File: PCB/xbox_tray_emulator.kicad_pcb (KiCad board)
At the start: 2 copper layers, 10.2 x 26.4 mm, 4 parts, among them J1 to Xbox, U1 ATtiny13A-S

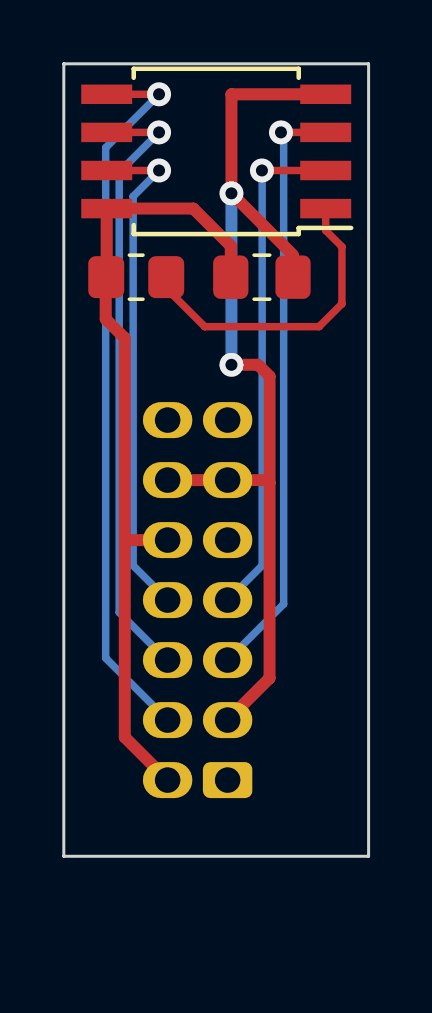
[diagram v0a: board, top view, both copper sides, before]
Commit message: reduce sleep current from 200uA to 50uA
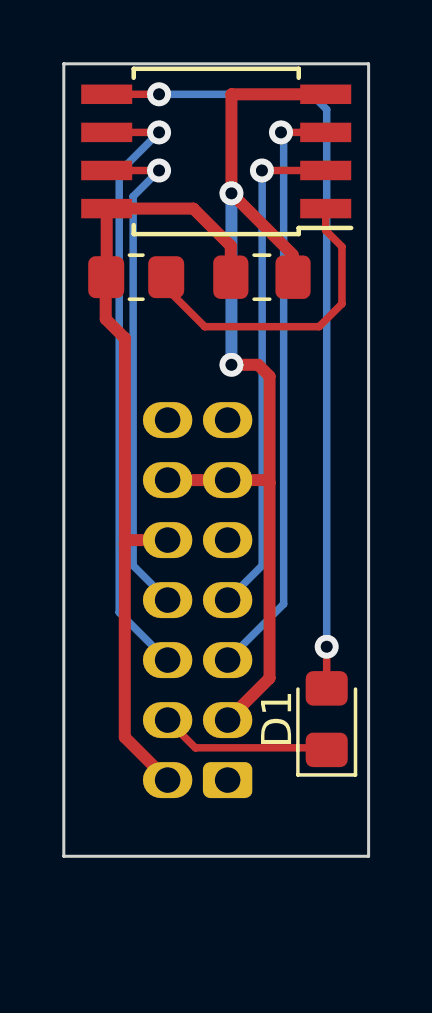
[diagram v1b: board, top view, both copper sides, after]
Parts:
- added D1: 1N4148, Diode_SMD:D_0805_2012Metric_Pad1.15x1.40mm_HandSolder, F.Cu at (145.9, 78.6)
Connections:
- J1 pad 4: Net-(J1-Pad4) -> Net-(D1-Pad1)
- U1 pad 5: Net-(J1-Pad4) -> Net-(D1-Pad2)
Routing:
- net Net-(D1-Pad2): track 0.00 -> 26.8 mm, vias 0 -> 2
- net Net-(J1-Pad4): track 24.2 -> 0.00 mm, vias 1 -> 0
- net Net-(D1-Pad1): track 0.00 -> 5.71 mm
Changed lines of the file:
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@@
   (net 4 "unconnected-(J1-Pad9)")
   (net 5 "unconnected-(J1-Pad13)")
-  (net 6 "Net-(J1-Pad4)")
+  (net 6 "Net-(D1-Pad1)")
   (net 7 "Net-(J1-Pad5)")
   (net 8 "Net-(J1-Pad6)")
@@
   (net 10 "Net-(J1-Pad8)")
   (net 11 "Net-(R1-Pad1)")
+  (net 12 "Net-(D1-Pad2)")
   (footprint "Capacitor_SMD:C_0805_2012Metric_Pad1.18x1.45mm_HandSolder" (layer "F.Cu")
     (at 143.764 63.881 180)
@@
       (net 2 "Net-(C1-Pad2)") (pintype "passive"))
     (model "${KICAD6_3DMODEL_DIR}/Capacitor_SMD.3dshapes/C_0805_2012Metric.wrl"
+      (offset (xyz 0 0 0))
+      (scale (xyz 1 1 1))
+      (rotate (xyz 0 0 0))
+    )
+  )
+  (footprint "Diode_SMD:D_0805_2012Metric_Pad1.15x1.40mm_HandSolder" (layer "F.Cu")
+    (at 145.923 78.613 90)
+    (descr "Diode SMD 0805 (2012 Metric), square (rectangular) end terminal, IPC_7351 nominal, (Body size source: https://docs.google.com/spreadsheets/d/1BsfQQcO9C6DZCsRaXUlFlo91Tg2WpOkGARC1WS5S8t0/edit?usp=sharing), generated with kicad-footprint-generator")
+    (tags "diode handsolder")
+    (property "Sheetfile" "xbox_tray_emulator.kicad_sch")
+    (property "Sheetname" "")
+    (attr smd)
+    (fp_text reference "D1" (at 0 -1.65 90) (layer "F.SilkS")
+      (effects (font (size 1 1) (thickness 0.15)))
+    )
+    (fp_text value "1N4148" (at 0 1.65 90) (layer "F.Fab")
+      (effects (font (size 1 1) (thickness 0.15)))
+    )
+    (fp_text user "${REFERENCE}" (at 0 0 90) (layer "F.Fab")
+      (effects (font (size 0.5 0.5) (thickness 0.08)))
+    )
+    (fp_line (start -1.86 -0.96) (end -1.86 0.96) (layer "F.SilkS") (width 0.12))
+    (fp_line (start 1 -0.96) (end -1.86 -0.96) (layer "F.SilkS") (width 0.12))
+    (fp_line (start -1.86 0.96) (end 1 0.96) (layer "F.SilkS") (width 0.12))
+    (fp_line (start 1.85 -0.95) (end 1.85 0.95) (layer "F.CrtYd") (width 0.05))
+    (fp_line (start 1.85 0.95) (end -1.85 0.95) (layer "F.CrtYd") (width 0.05))
+    (fp_line (start -1.85 0.95) (end -1.85 -0.95) (layer "F.CrtYd") (width 0.05))
+    (fp_line (start -1.85 -0.95) (end 1.85 -0.95) (layer "F.CrtYd") (width 0.05))
+    (fp_line (start 1 0.6) (end 1 -0.6) (layer "F.Fab") (width 0.1))
+    (fp_line (start -1 0.6) (end 1 0.6) (layer "F.Fab") (width 0.1))
+    (fp_line (start 1 -0.6) (end -0.7 -0.6) (layer "F.Fab") (width 0.1))
+    (fp_line (start -0.7 -0.6) (end -1 -0.3) (layer "F.Fab") (width 0.1))
+    (fp_line (start -1 -0.3) (end -1 0.6) (layer "F.Fab") (width 0.1))
+    (pad "1" smd roundrect (at -1.025 0 90) (size 1.15 1.4) (layers "F.Cu" "F.Paste" "F.Mask") (roundrect_rratio 0.217391)
+      (net 6 "Net-(D1-Pad1)") (pinfunction "K") (pintype "passive"))
+    (pad "2" smd roundrect (at 1.025 0 90) (size 1.15 1.4) (layers "F.Cu" "F.Paste" "F.Mask") (roundrect_rratio 0.217391)
+      (net 12 "Net-(D1-Pad2)") (pinfunction "A") (pintype "passive"))
+    (model "${KICAD6_3DMODEL_DIR}/Diode_SMD.3dshapes/D_0805_2012Metric.wrl"
       (offset (xyz 0 0 0))
       (scale (xyz 1 1 1))
@@
       (net 1 "Net-(C1-Pad1)") (pinfunction "GND") (pintype "power_in"))
     (pad "5" smd rect (at 3.65 1.905 180) (size 1.7 0.65) (layers "F.Cu" "F.Paste" "F.Mask")
-      (net 6 "Net-(J1-Pad4)") (pinfunction "PB0") (pintype "bidirectional"))
+      (net 12 "Net-(D1-Pad2)") (pinfunction "PB0") (pintype "bidirectional"))
     (pad "6" smd rect (at 3.65 0.635 180) (size 1.7 0.65) (layers "F.Cu" "F.Paste" "F.Mask")
       (net 8 "Net-(J1-Pad6)") (pinfunction "PB1") (pintype "bidirectional"))
@@
       (net 1 "Net-(C1-Pad1)") (pinfunction "Pin_3") (pintype "passive"))
     (pad "4" thru_hole oval (at 2 -2 90) (size 1.2 1.65) (drill 0.85) (layers *.Cu *.Mask)
-      (net 6 "Net-(J1-Pad4)") (pinfunction "Pin_4") (pintype "passive"))
+      (net 6 "Net-(D1-Pad1)") (pinfunction "Pin_4") (pintype "passive"))
     (pad "5" thru_hole oval (at 4 0 90) (size 1.2 1.65) (drill 0.85) (layers *.Cu *.Mask)
       (net 7 "Net-(J1-Pad5)") (pinfunction "Pin_5") (pintype "passive"))
@@
   (segment (start 139.192 65.913) (end 139.192 79.216) (width 0.4) (layer "F.Cu") (net 2))
   (segment (start 142.7265 62.8435) (end 141.478 61.595) (width 0.4) (layer "F.Cu") (net 2))
-  (segment (start 138.59 57.785) (end 140.335 57.785) (width 0.25) (layer "F.Cu") (net 6))
-  (via (at 140.335 57.785) (size 0.8) (drill 0.4) (layers "F.Cu" "B.Cu") (net 6))
-  (segment (start 138.557 76.581) (end 140.621 78.645) (width 0.25) (layer "B.Cu") (net 6))
-  (segment (start 138.557 59.563) (end 138.557 76.581) (width 0.25) (layer "B.Cu") (net 6))
-  (segment (start 140.335 57.785) (end 138.557 59.563) (width 0.25) (layer "B.Cu") (net 6))
+  (segment (start 140.621 78.645) (end 141.54552 79.56952) (width 0.25) (layer "F.Cu") (net 6))
+  (segment (start 145.85452 79.56952) (end 145.923 79.638) (width 0.25) (layer "F.Cu") (net 6))
+  (segment (start 141.54552 79.56952) (end 145.85452 79.56952) (width 0.25) (layer "F.Cu") (net 6))
   (segment (start 145.89 59.055) (end 144.399 59.055) (width 0.25) (layer "F.Cu") (net 7))
   (via (at 144.399 59.055) (size 0.8) (drill 0.4) (layers "F.Cu" "B.Cu") (net 7))
@@
   (segment (start 141.859 65.532) (end 140.573 64.246) (width 0.25) (layer "F.Cu") (net 11))
   (segment (start 145.669 65.532) (end 141.859 65.532) (width 0.25) (layer "F.Cu") (net 11))
+  (segment (start 145.923 77.588) (end 145.923 76.2) (width 0.25) (layer "F.Cu") (net 12))
+  (segment (start 138.59 57.785) (end 140.335 57.785) (width 0.25) (layer "F.Cu") (net 12))
+  (via (at 145.923 76.2) (size 0.8) (drill 0.4) (layers "F.Cu" "B.Cu") (net 12))
+  (via (at 140.335 57.785) (size 0.8) (drill 0.4) (layers "F.Cu" "B.Cu") (net 12))
+  (segment (start 145.923 76.2) (end 145.923 58.293) (width 0.25) (layer "B.Cu") (net 12))
+  (segment (start 145.415 57.785) (end 140.335 57.785) (width 0.25) (layer "B.Cu") (net 12))
+  (segment (start 145.923 58.293) (end 145.415 57.785) (width 0.25) (layer "B.Cu") (net 12))
 )

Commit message: Xbox DVD logic levels are 3.3v, a 3.3v regulator was added to the PCB so the ATtiny13a will output and accept 3.3v logic. ATtiny13a sleep current draw is now a fration of a uA. modify tray open sequence to closer approximate a real DVD drive.
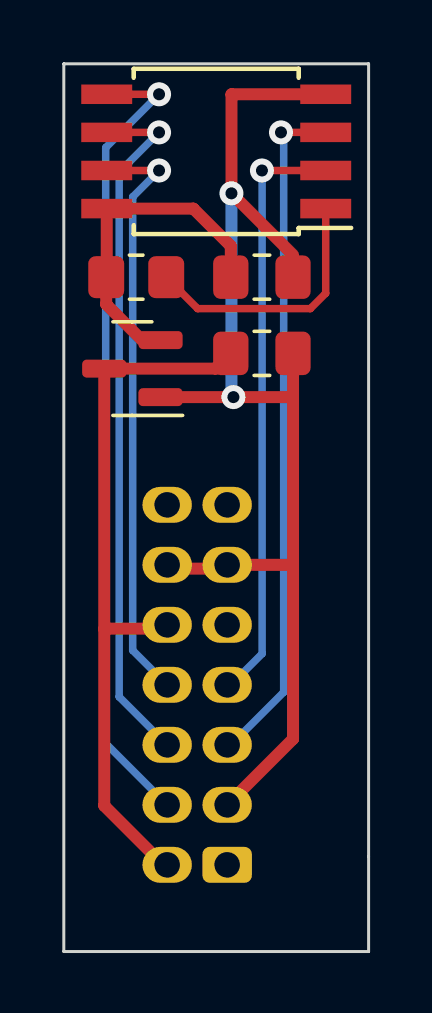
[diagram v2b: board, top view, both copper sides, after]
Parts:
- removed D1: 1N4148, Diode_SMD:D_0805_2012Metric_Pad1.15x1.40mm_HandSolder
- added C2: 1uf, Capacitor_SMD:C_0805_2012Metric_Pad1.18x1.45mm_HandSolder, F.Cu at (143.8, 66.4)
- added U2: AP2127N-3.3, Package_TO_SOT_SMD:SOT-23, F.Cu at (139.4, 66.9)
- C1: value 0.47uf -> 4.7uf
- moved J1 2.83 mm to (142.6, 83.5)
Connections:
- J1 pad 10: Net-(C1-Pad2) -> Net-(J1-Pad10)
- J1 pad 2: Net-(C1-Pad2) -> Net-(J1-Pad10)
- J1 pad 4: Net-(D1-Pad1) -> Net-(J1-Pad4)
- U1 pad 5: Net-(D1-Pad2) -> Net-(J1-Pad4)
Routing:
- net Net-(J1-Pad4): track 0.00 -> 27.0 mm, vias 0 -> 1
- net Net-(D1-Pad2): track 26.8 -> 0.00 mm, vias 2 -> 0
- net Net-(J1-Pad10): track 0.00 -> 24.1 mm
- net Net-(C1-Pad2): track 27.1 -> 11.4 mm
- net Net-(C1-Pad1): track 32.7 -> 41.3 mm
- net Net-(D1-Pad1): track 5.71 -> 0.00 mm
- net Net-(J1-Pad7): track 16.9 -> 19.9 mm
- net Net-(J1-Pad5): track 19.9 -> 22.9 mm
- net Net-(J1-Pad8): track 16.9 -> 19.7 mm
- net Net-(J1-Pad6): track 20.6 -> 23.4 mm
- net Net-(R1-Pad1): track 10.5 -> 8.79 mm
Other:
- board size 10.2 x 26.4 mm -> 10.2 x 29.6 mm

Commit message: add ground fill
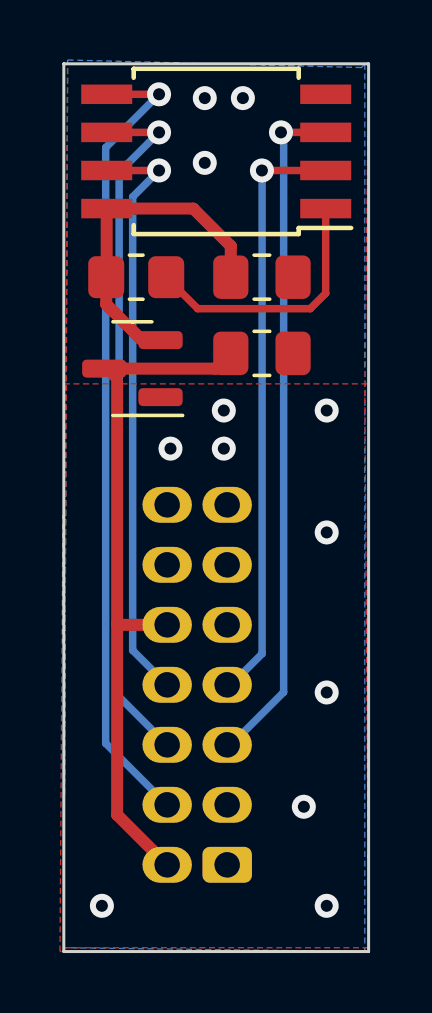
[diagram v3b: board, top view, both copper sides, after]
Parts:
- C1: value 4.7uf -> 1uf
- turned C1 to 0 degrees
- turned R1 to 0 degrees
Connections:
- C1 pad 1: Net-(C1-Pad1) -> /Net-(R1-Pad1)
- C2 pad 2: Net-(C1-Pad1) -> Net-(C1-Pad2)
- J1 pad 11: Net-(C1-Pad1) -> Net-(C1-Pad2)
- J1 pad 12: Net-(C1-Pad1) -> Net-(C1-Pad2)
- J1 pad 3: Net-(C1-Pad1) -> Net-(C1-Pad2)
- R1 pad 1: Net-(R1-Pad1) -> /Net-(R1-Pad1)
- R1 pad 2: Net-(C1-Pad2) -> Net-(R1-Pad2)
- U1 pad 1: Net-(R1-Pad1) -> Net-(R1-Pad2)
- U1 pad 4: Net-(C1-Pad1) -> Net-(C1-Pad2)
- U1 pad 8: Net-(C1-Pad2) -> /Net-(R1-Pad1)
- U2 pad 1: Net-(C1-Pad1) -> Net-(C1-Pad2)
- U2 pad 2: Net-(C1-Pad2) -> /Net-(R1-Pad1)
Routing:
- net Net-(C1-Pad1): track 41.3 -> 0.00 mm, vias 2 -> 0
- net Net-(C1-Pad2): track 11.4 -> 0.00 mm, vias 0 -> 12
- net /Net-(R1-Pad1): track 0.00 -> 11.4 mm
- net Net-(R1-Pad2): track 0.00 -> 8.79 mm
- net Net-(R1-Pad1): track 8.79 -> 0.00 mm
- net /Net-(J1-Pad10): track 24.1 -> 23.5 mm
- added copper zone on B.Cu, net Net-(C1-Pad2)
- added copper zone on F.Cu, net Net-(C1-Pad2)

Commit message: increase U1 pads for "narrow" ATtiny13
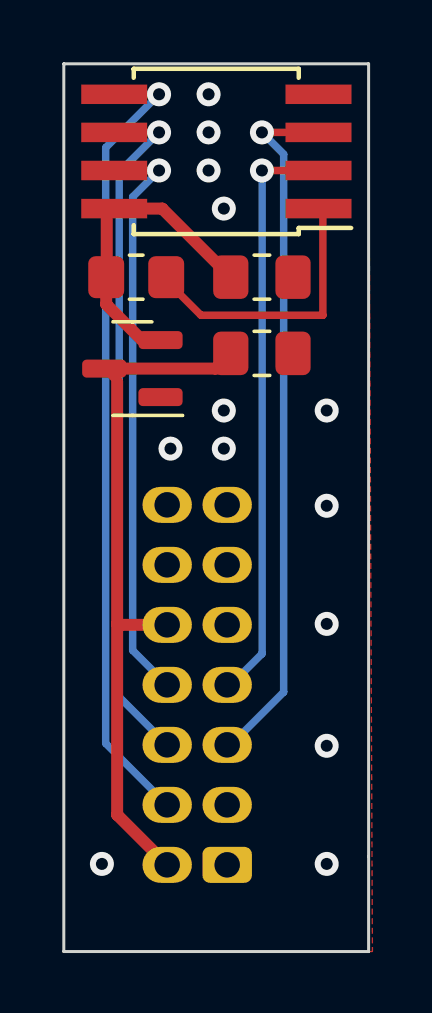
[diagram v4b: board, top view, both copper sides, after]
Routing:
- net /Net-(R1-Pad1): track 11.4 -> 10.6 mm
- net Net-(J1-Pad5): track 22.9 -> 23.5 mm
- net Net-(R1-Pad2): track 8.79 -> 9.43 mm
- net Net-(C1-Pad2): vias 12 -> 13
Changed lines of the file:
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@@
     (fp_line (start -2.65 2.65) (end -2.65 -1.65) (layer "F.Fab") (width 0.15))
     (fp_line (start 2.65 2.65) (end -2.65 2.65) (layer "F.Fab") (width 0.15))
-    (pad "1" smd rect (at -3.65 -1.905 180) (size 1.7 0.65) (layers "F.Cu" "F.Paste" "F.Mask")
+    (pad "1" smd rect (at -3.41 -1.905 180) (size 2.2 0.65) (layers "F.Cu" "F.Paste" "F.Mask")
       (net 9 "Net-(R1-Pad2)") (pinfunction "~{RESET}/PB5") (pintype "bidirectional"))
-    (pad "2" smd rect (at -3.65 -0.635 180) (size 1.7 0.65) (layers "F.Cu" "F.Paste" "F.Mask")
+    (pad "2" smd rect (at -3.41 -0.635 180) (size 2.2 0.65) (layers "F.Cu" "F.Paste" "F.Mask")
       (net 6 "Net-(J1-Pad7)") (pinfunction "PB3") (pintype "bidirectional"))
-    (pad "3" smd rect (at -3.65 0.635 180) (size 1.7 0.65) (layers "F.Cu" "F.Paste" "F.Mask")
+    (pad "3" smd rect (at -3.41 0.635 180) (size 2.2 0.65) (layers "F.Cu" "F.Paste" "F.Mask")
       (net 4 "Net-(J1-Pad5)") (pinfunction "PB4") (pintype "bidirectional"))
-    (pad "4" smd rect (at -3.65 1.905 180) (size 1.7 0.65) (layers "F.Cu" "F.Paste" "F.Mask")
+    (pad "4" smd rect (at -3.41 1.905 180) (size 2.2 0.65) (layers "F.Cu" "F.Paste" "F.Mask")
       (net 12 "Net-(C1-Pad2)") (pinfunction "GND") (pintype "power_in"))
-    (pad "5" smd rect (at 3.65 1.905 180) (size 1.7 0.65) (layers "F.Cu" "F.Paste" "F.Mask")
+    (pad "5" smd rect (at 3.4 1.905 180) (size 2.2 0.65) (layers "F.Cu" "F.Paste" "F.Mask")
       (net 8 "Net-(J1-Pad4)") (pinfunction "PB0") (pintype "bidirectional"))
-    (pad "6" smd rect (at 3.65 0.635 180) (size 1.7 0.65) (layers "F.Cu" "F.Paste" "F.Mask")
+    (pad "6" smd rect (at 3.4 0.635 180) (size 2.2 0.65) (layers "F.Cu" "F.Paste" "F.Mask")
       (net 5 "Net-(J1-Pad6)") (pinfunction "PB1") (pintype "bidirectional"))
-    (pad "7" smd rect (at 3.65 -0.635 180) (size 1.7 0.65) (layers "F.Cu" "F.Paste" "F.Mask")
+    (pad "7" smd rect (at 3.4 -0.635 180) (size 2.2 0.65) (layers "F.Cu" "F.Paste" "F.Mask")
       (net 7 "Net-(J1-Pad8)") (pinfunction "PB2") (pintype "bidirectional"))
-    (pad "8" smd rect (at 3.65 -1.905 180) (size 1.7 0.65) (layers "F.Cu" "F.Paste" "F.Mask")
+    (pad "8" smd rect (at 3.4 -1.905 180) (size 2.2 0.65) (layers "F.Cu" "F.Paste" "F.Mask")
       (net 10 "/Net-(R1-Pad1)") (pinfunction "VCC") (pintype "power_in"))
     (model "${KICAD6_3DMODEL_DIR}/Package_SO.3dshapes/SOIC-8W_5.3x5.3mm_P1.27mm.wrl"
@@
   (gr_line (start 147.32 83.185) (end 147.32 86.36) (layer "Edge.Cuts") (width 0.1))
   (gr_line (start 147.32 56.769) (end 147.32 83.185) (layer "Edge.Cuts") (width 0.1))
-  (segment (start 145.89 59.055) (end 144.399 59.055) (width 0.25) (layer "F.Cu") (net 4))
-  (via (at 144.399 59.055) (size 0.8) (drill 0.4) (layers "F.Cu" "B.Cu") (net 4))
+  (segment (start 145.65 59.055) (end 143.764 59.055) (width 0.25) (layer "F.Cu") (net 4))
+  (via (at 143.764 59.055) (size 0.8) (drill 0.4) (layers "F.Cu" "B.Cu") (net 4))
+  (segment (start 144.488511 77.713489) (end 144.488511 59.779511) (width 0.25) (layer "B.Cu") (net 4))
   (segment (start 144.488511 77.713489) (end 142.605 79.597) (width 0.25) (layer "B.Cu") (net 4))
-  (segment (start 144.399 59.055) (end 144.488511 59.144511) (width 0.25) (layer "B.Cu") (net 4))
-  (segment (start 144.488511 59.144511) (end 144.488511 77.713489) (width 0.25) (layer "B.Cu") (net 4))
+  (segment (start 144.488511 59.779511) (end 143.764 59.055) (width 0.25) (layer "B.Cu") (net 4))
   (segment (start 138.59 59.055) (end 140.335 59.055) (width 0.25) (layer "F.Cu") (net 5))
   (via (at 140.335 59.055) (size 0.8) (drill 0.4) (layers "F.Cu" "B.Cu") (net 5))
@@
   (segment (start 138.55644 59.56356) (end 138.55644 79.42144) (width 0.25) (layer "B.Cu") (net 8))
   (segment (start 140.335 57.785) (end 138.55644 59.56356) (width 0.25) (layer "B.Cu") (net 8))
-  (segment (start 141.62252 64.93052) (end 140.573 63.881) (width 0.25) (layer "F.Cu") (net 9))
-  (segment (start 145.89 64.417493) (end 145.89 61.595) (width 0.25) (layer "F.Cu") (net 9))
-  (segment (start 145.376973 64.93052) (end 145.89 64.417493) (width 0.25) (layer "F.Cu") (net 9))
-  (segment (start 141.62252 64.93052) (end 145.376973 64.93052) (width 0.25) (layer "F.Cu") (net 9))
-  (segment (start 142.7265 63.881) (end 142.7265 62.8435) (width 0.4) (layer "F.Cu") (net 10))
+  (segment (start 145.796 65.151) (end 145.796 61.741) (width 0.25) (layer "F.Cu") (net 9))
+  (segment (start 140.573 63.881) (end 140.573 63.992) (width 0.25) (layer "F.Cu") (net 9))
+  (segment (start 145.796 61.741) (end 145.65 61.595) (width 0.25) (layer "F.Cu") (net 9))
+  (segment (start 141.732 65.151) (end 145.796 65.151) (width 0.25) (layer "F.Cu") (net 9))
+  (segment (start 140.573 63.992) (end 141.732 65.151) (width 0.25) (layer "F.Cu") (net 9))
   (segment (start 138.557 63.897) (end 138.573 63.881) (width 0.4) (layer "F.Cu") (net 10))
   (segment (start 139.766 65.979) (end 138.573 64.786) (width 0.4) (layer "F.Cu") (net 10))
+  (segment (start 140.4405 61.595) (end 138.84 61.595) (width 0.4) (layer "F.Cu") (net 10))
   (segment (start 138.59 64.118) (end 138.59 61.595) (width 0.4) (layer "F.Cu") (net 10))
-  (segment (start 141.478 61.595) (end 138.59 61.595) (width 0.4) (layer "F.Cu") (net 10))
-  (segment (start 142.7265 62.8435) (end 141.478 61.595) (width 0.4) (layer "F.Cu") (net 10))
+  (segment (start 142.7265 63.881) (end 140.4405 61.595) (width 0.4) (layer "F.Cu") (net 10))
   (segment (start 138.573 64.786) (end 138.573 63.881) (width 0.4) (layer "F.Cu") (net 10))
   (segment (start 140.3835 65.979) (end 139.766 65.979) (width 0.25) (layer "F.Cu") (net 10))
@@
   (segment (start 140.605 83.47) (end 138.938 81.803) (width 0.4) (layer "F.Cu") (net 11))
   (segment (start 142.2185 66.929) (end 142.7265 66.421) (width 0.4) (layer "F.Cu") (net 11))
-  (via (at 141.859 60.071) (size 0.8) (drill 0.4) (layers "F.Cu" "B.Cu") (free) (net 12))
-  (via (at 145.923 84.836) (size 0.8) (drill 0.4) (layers "F.Cu" "B.Cu") (free) (net 12))
-  (via (at 145.923 72.39) (size 0.8) (drill 0.4) (layers "F.Cu" "B.Cu") (free) (net 12))
+  (via (at 142.494 61.595) (size 0.8) (drill 0.4) (layers "F.Cu" "B.Cu") (free) (net 12))
+  (via (at 141.986 57.785) (size 0.8) (drill 0.4) (layers "F.Cu" "B.Cu") (free) (net 12))
+  (via (at 145.923 71.501) (size 0.8) (drill 0.4) (layers "F.Cu" "B.Cu") (free) (net 12))
+  (via (at 138.43 83.439) (size 0.8) (drill 0.4) (layers "F.Cu" "B.Cu") (free) (net 12))
   (via (at 142.494 68.326) (size 0.8) (drill 0.4) (layers "F.Cu" "B.Cu") (free) (net 12))
-  (via (at 143.129 57.912) (size 0.8) (drill 0.4) (layers "F.Cu" "B.Cu") (free) (net 12))
   (via (at 142.494 69.596) (size 0.8) (drill 0.4) (layers "F.Cu" "B.Cu") (free) (net 12))
-  (via (at 138.43 84.836) (size 0.8) (drill 0.4) (layers "F.Cu" "B.Cu") (free) (net 12))
-  (via (at 145.923 77.724) (size 0.8) (drill 0.4) (layers "F.Cu" "B.Cu") (free) (net 12))
-  (via (at 145.161 81.534) (size 0.8) (drill 0.4) (layers "F.Cu" "B.Cu") (free) (net 12))
-  (via (at 141.859 57.912) (size 0.8) (drill 0.4) (layers "F.Cu" "B.Cu") (free) (net 12))
+  (via (at 141.986 59.055) (size 0.8) (drill 0.4) (layers "F.Cu" "B.Cu") (free) (net 12))
+  (via (at 145.923 79.502) (size 0.8) (drill 0.4) (layers "F.Cu" "B.Cu") (free) (net 12))
+  (via (at 145.923 83.439) (size 0.8) (drill 0.4) (layers "F.Cu" "B.Cu") (free) (net 12))
   (via (at 140.716 69.596) (size 0.8) (drill 0.4) (layers "F.Cu" "B.Cu") (free) (net 12))
   (via (at 145.923 68.326) (size 0.8) (drill 0.4) (layers "F.Cu" "B.Cu") (free) (net 12))
+  (via (at 145.923 75.438) (size 0.8) (drill 0.4) (layers "F.Cu" "B.Cu") (free) (net 12))
+  (via (at 141.986 60.325) (size 0.8) (drill 0.4) (layers "F.Cu" "B.Cu") (free) (net 12))
   (zone (net 12) (net_name "Net-(C1-Pad2)") (layer "F.Cu") (hatch edge 0.508)
-    (connect_pads (clearance 0.508))
+    (connect_pads yes (clearance 0.508))
+    (min_thickness 0.254) (filled_areas_thickness no)
+    (fill yes (thermal_gap 0.508) (thermal_bridge_width 0.508))
+    (polygon
+      (pts
+        (xy 147.447 86.36)
+        (xy 137.16 86.36)
+        (xy 137.16 56.769)
+        (xy 147.32 56.769)
+      )
+    )
+  )
+  (zone (net 12) (net_name "Net-(C1-Pad2)") (layer "B.Cu") (hatch edge 0.508)
+    (connect_pads yes (clearance 0.508))
     (min_thickness 0.254) (filled_areas_thickness no)
     (fill yes (thermal_gap 0.508) (thermal_bridge_width 0.508))
@@
       (pts
         (xy 147.32 86.36)
-        (xy 137.033 86.36)
-        (xy 137.16 67.437)
-        (xy 147.32 67.437)
-      )
-    )
-  )
-  (zone (net 12) (net_name "Net-(C1-Pad2)") (layer "F.Cu") (hatch edge 0.508)
-    (connect_pads thru_hole_only (clearance 0.508))
-    (min_thickness 0.254) (filled_areas_thickness no)
-    (fill yes (thermal_gap 0.508) (thermal_bridge_width 0.508))
-    (polygon
-      (pts
-        (xy 147.193545 67.897034)
-        (xy 147.32 86.233)
-        (xy 137.16 86.233)
-        (xy 137.287 56.769)
+        (xy 137.16 86.36)
+        (xy 137.16 56.769)
         (xy 147.32 56.769)
       )
     )
-  )
-  (zone (net 12) (net_name "Net-(C1-Pad2)") (layer "B.Cu") (hatch edge 0.508)
-    (connect_pads thru_hole_only (clearance 0.508))
-    (min_thickness 0.254) (filled_areas_thickness no)
-    (fill yes (thermal_gap 0.508) (thermal_bridge_width 0.508))
-    (polygon
-      (pts
-        (xy 147.084703 56.893223)
-        (xy 147.193 56.769)
-        (xy 147.193 86.36)
-        (xy 137.16 86.233)
-        (xy 137.287 56.642)
-      )
-    )
